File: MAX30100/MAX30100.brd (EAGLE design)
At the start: 12.7 x 13.7 mm, 2 parts

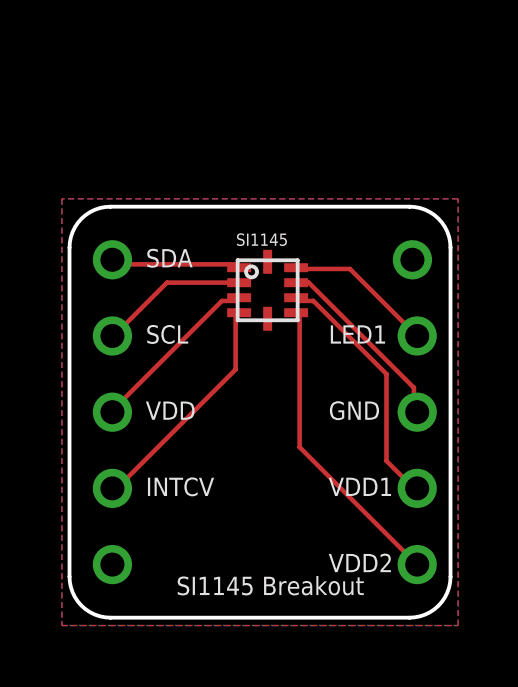
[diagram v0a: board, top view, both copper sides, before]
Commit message: Add breakout board
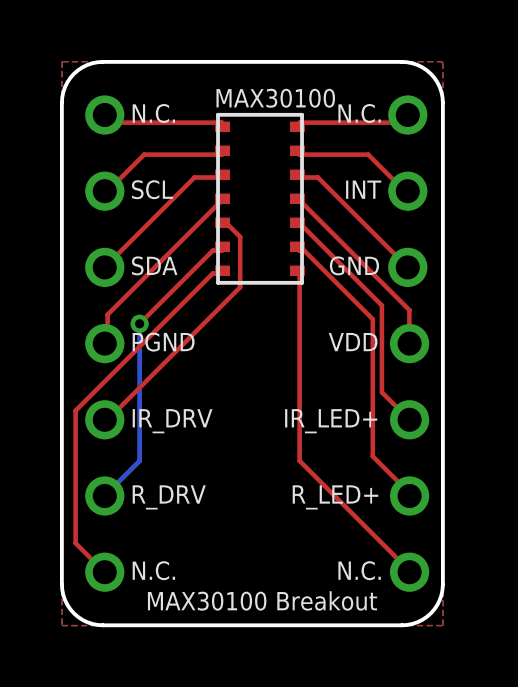
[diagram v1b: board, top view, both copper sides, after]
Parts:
- removed SI1145: SL-SI1145, FaBo-Mems:SILICONLABS-SI1145
- added MAX30100: MA-MAX30100, FaBo-Mems:MAXIM-30100
- U$2: value 10PIN -> 14PIN; device FaBo-Breakout:10PIN -> FaBo-Breakout:14PIN
- moved U$2 1.55 mm to (6.35, 9.40)
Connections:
- new net 11: MAX30100.11, U$2.11
- new net 12: MAX30100.12, U$2.12
- new net 13: MAX30100.13, U$2.13
- new net 14: MAX30100.14, U$2.14
- net 1: now also MAX30100.1; no longer SI1145.1
- net 10: now also MAX30100.10
- net 2: now also MAX30100.2; no longer SI1145.2
- net 3: now also MAX30100.3; no longer SI1145.3
- net 4: now also MAX30100.4; no longer SI1145.4
- net 5: now also MAX30100.5
- net 6: now also MAX30100.6; no longer SI1145.6
- net 7: now also MAX30100.7; no longer SI1145.7
- net 8: now also MAX30100.8; no longer SI1145.8
- net 9: now also MAX30100.9; no longer SI1145.9
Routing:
- net 5: track 0.00 -> 8.80 mm
- net 10: track 0.00 -> 8.15 mm
- net 11: track 0.00 -> 6.38 mm
- net 8: track 6.26 -> 11.6 mm
- net 9: track 4.97 -> 9.93 mm
- net 12: track 0.00 -> 4.96 mm
- net 7: track 8.36 -> 12.7 mm
- net 13: track 0.00 -> 4.26 mm
- net 14: track 0.00 -> 3.87 mm
- net 4: track 7.71 -> 6.46 mm
- net 3: track 5.84 -> 5.24 mm
- net 6: vias 0 -> 1
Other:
- board size 12.7 x 13.7 mm -> 12.7 x 18.8 mm
- board text added: "INT"
- board text added: "IR_DRV"
- board text added: "IR_LED+"
- board text added: "MAX30100 Breakout"
- board text added: "N.C."
- board text added: "PGND"
- board text added: "R_DRV"
- board text added: "R_LED+"
- board text removed: "INTCV"
- board text removed: "LED1"
- board text removed: "SI1145 Breakout"
- board text removed: "VDD1"
- board text removed: "VDD2"
